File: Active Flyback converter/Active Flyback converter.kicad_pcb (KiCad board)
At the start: 12 copper layers, 114.5 x 43 mm, 0 parts

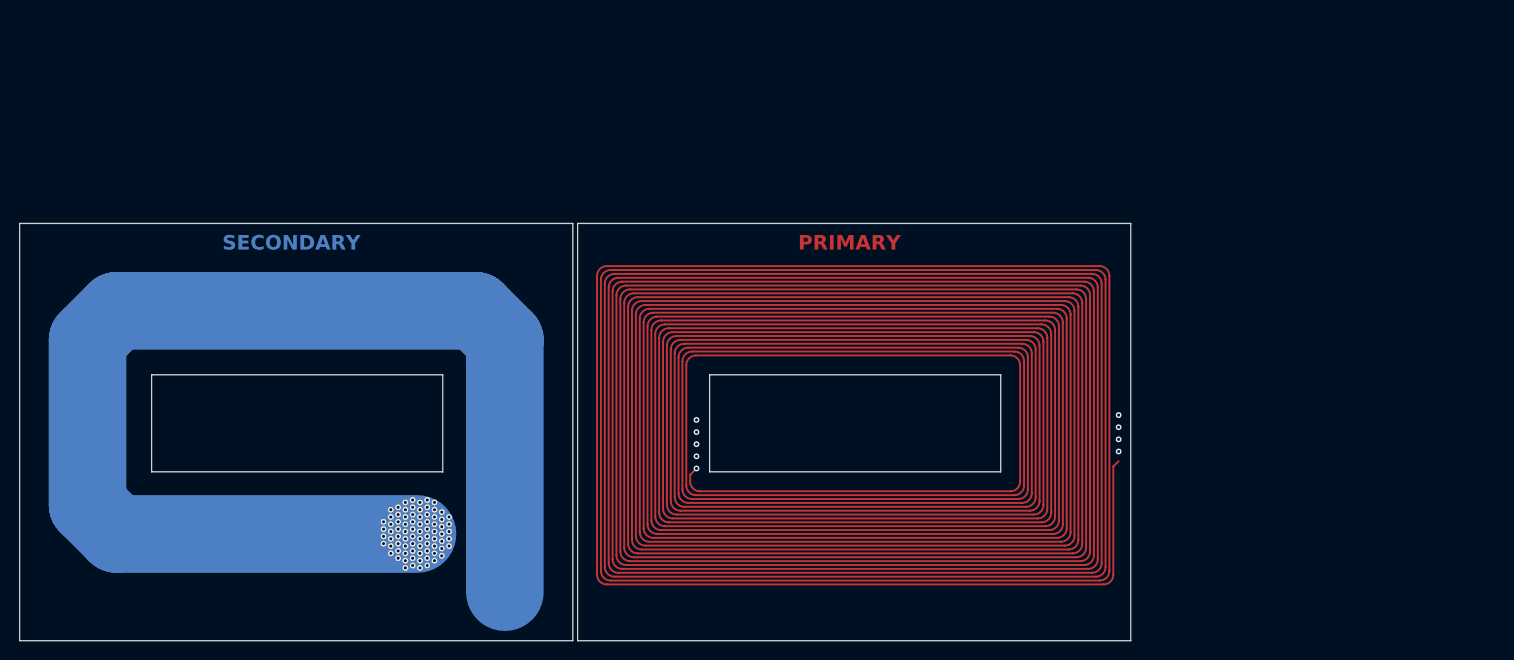
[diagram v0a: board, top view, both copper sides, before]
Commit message: Active flyback converter - v1.1
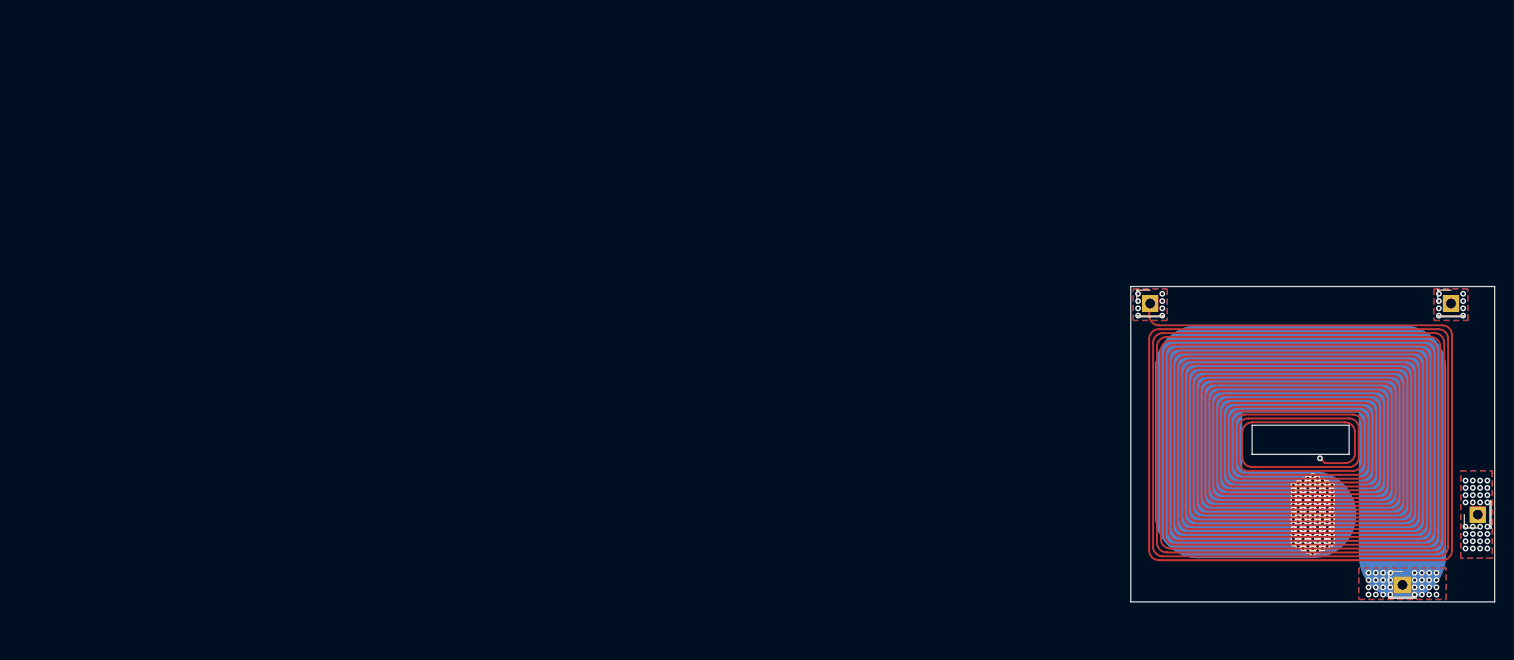
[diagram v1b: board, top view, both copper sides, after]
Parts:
- added J1: Conn_01x01_Pin, Connector_PinHeader_2.54mm:PinHeader_1x01_P2.54mm_Vertical, F.Cu at (157.0, 64.2)
- added J2: Conn_01x01_Pin, Connector_PinHeader_2.54mm:PinHeader_1x01_P2.54mm_Vertical, F.Cu at (190.8, 86.0)
- added J3: Conn_01x01_Pin, Connector_PinHeader_2.54mm:PinHeader_1x01_P2.54mm_Vertical, F.Cu at (188.0, 64.2)
- added J7: Conn_01x01_Pin, Connector_PinHeader_2.54mm:PinHeader_1x01_P2.54mm_Vertical, F.Cu at (183.0, 93.2)
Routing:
- net (no net): track 32506.6 -> 0.00 mm, vias 89 -> 0
- net /primary: track 0.00 -> 17714.3 mm, vias 0 -> 25
- net /secondary: track 0.00 -> 81.0 mm, vias 0 -> 197
- added copper zone on B.Cu, net /primary
- added copper zone on F.Cu, net /primary
- added copper zone on In1.Cu, net /primary
- added copper zone on In10.Cu, net /primary
- added copper zone on In2.Cu, net /primary
- added copper zone on In3.Cu, net /primary
- added copper zone on In4.Cu, net /primary
- added copper zone on In5.Cu, net /primary
- added copper zone on In6.Cu, net /primary
- added copper zone on In7.Cu, net /primary
- added copper zone on In8.Cu, net /primary
- added copper zone on In9.Cu, net /primary
- added copper zone on B.Cu, net /secondary
- added copper zone on F.Cu, net /secondary
- added copper zone on In1.Cu, net /secondary
- added copper zone on In10.Cu, net /secondary
- added copper zone on In2.Cu, net /secondary
- added copper zone on In3.Cu, net /secondary
- added copper zone on In4.Cu, net /secondary
- added copper zone on In5.Cu, net /secondary
- added copper zone on In6.Cu, net /secondary
- added copper zone on In7.Cu, net /secondary
- added copper zone on In8.Cu, net /secondary
- added copper zone on In9.Cu, net /secondary
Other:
- board size 114.5 x 43 mm -> 37.5 x 32.5 mm
- board text added: "250:1 planar transformer for 2.5V & 10A output. 1200V --> 2.1V 10A, 250KHz, 30% duty Np/Ns = (Vin * D) / (Vout * (1 - D)) = 245 Np = 245 turns, Ns = 1 turn L = ((u0 * N^2 * A) / l) Where... u0 = 4 * pi * 10^(-7) N = 250 (25 turns x 10 layers) A = 0.0325m x 0.01225m l = 0.0016m Thus, L = 19.543mH"
- board text removed: "PRIMARY"
- board text removed: "SECONDARY"

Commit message: Active flyback converter - v1.2
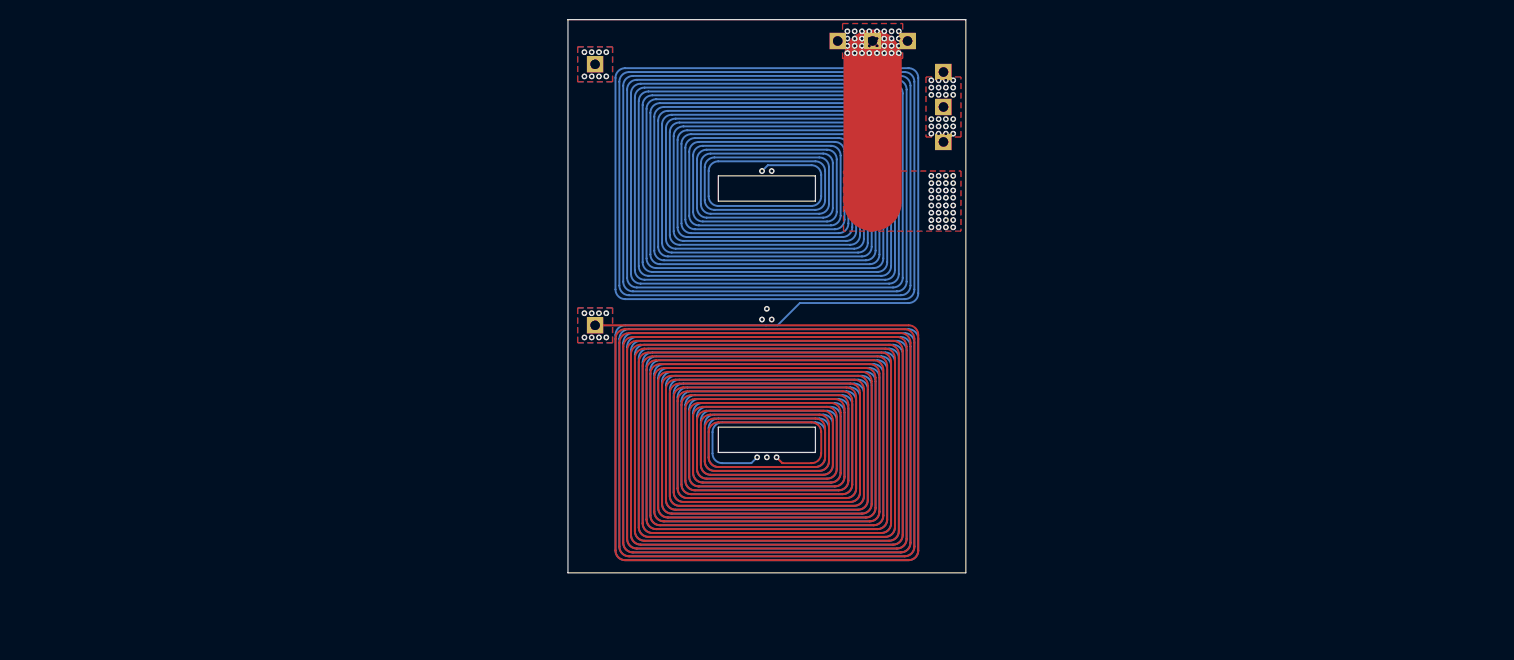
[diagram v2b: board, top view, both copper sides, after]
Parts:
- added J4: Conn_01x01_Pin, Connector_PinHeader_2.54mm:PinHeader_1x01_P2.54mm_Vertical, B.Cu at (135.7, 40.4)
- added J5: Conn_01x01_Pin, Connector_PinHeader_2.54mm:PinHeader_1x01_P2.54mm_Vertical, B.Cu at (135.7, 47.6)
- added J6: Conn_01x01_Pin, Connector_PinHeader_2.54mm:PinHeader_1x01_P2.54mm_Vertical, B.Cu at (132.0, 37.2)
- added J8: Conn_01x01_Pin, Connector_PinHeader_2.54mm:PinHeader_1x01_P2.54mm_Vertical, B.Cu at (124.8, 37.2)
- J1, J2, J3, J7: moved to B.Cu
- moved J3 91.6 mm to (99.8, 39.6), turned to 90 degrees
- moved J2 79.2 mm to (128.4, 37.2), turned to 0 degrees
- moved J7 68.3 mm to (135.7, 44.0), turned to 90 degrees
- moved J1 57.2 mm to (99.8, 66.5), turned to 90 degrees
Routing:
- net /primary: track 17714.3 -> 17771.2 mm, vias 25 -> 24
- net /secondary: track 81.0 -> 84.7 mm, vias 197 -> 88
- removed copper zone on In10.Cu, net /primary
- removed copper zone on In5.Cu, net /primary
- removed copper zone on In6.Cu, net /primary
- removed copper zone on In7.Cu, net /primary
- removed copper zone on In8.Cu, net /primary
- removed copper zone on In9.Cu, net /primary
- removed copper zone on B.Cu, net /secondary
- removed copper zone on In10.Cu, net /secondary
- removed copper zone on In2.Cu, net /secondary
- removed copper zone on In3.Cu, net /secondary
- removed copper zone on In4.Cu, net /secondary
- removed copper zone on In5.Cu, net /secondary
- removed copper zone on In6.Cu, net /secondary
- removed copper zone on In7.Cu, net /secondary
- removed copper zone on In8.Cu, net /secondary
- removed copper zone on In9.Cu, net /secondary
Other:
- board size 37.5 x 32.5 mm -> 41 x 57 mm
- copper layers 12 -> 6

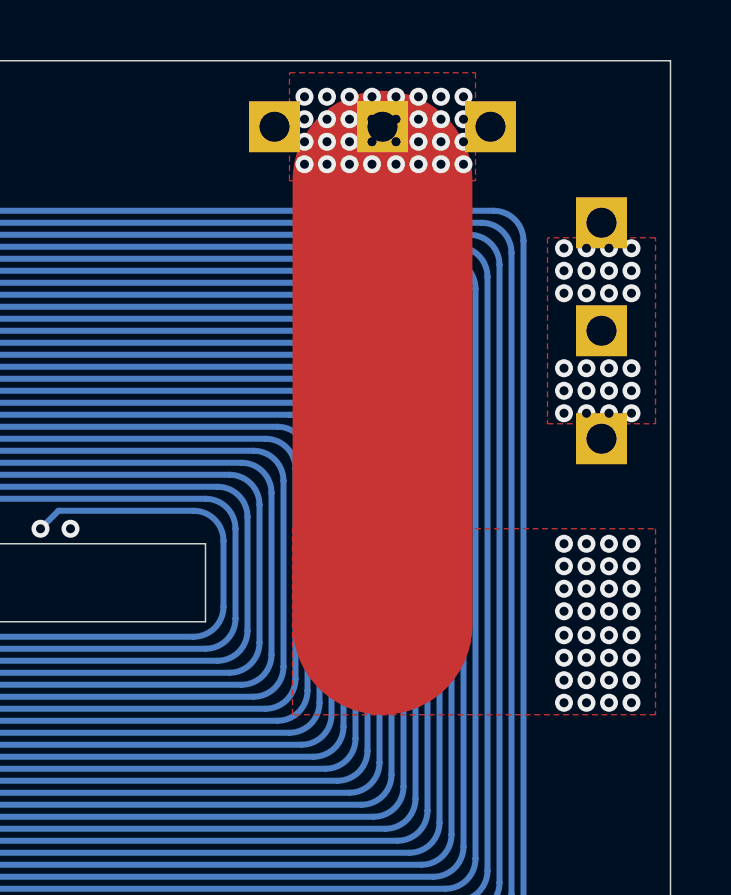
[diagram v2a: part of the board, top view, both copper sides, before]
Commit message: Active flyback converter (actual v1.2)
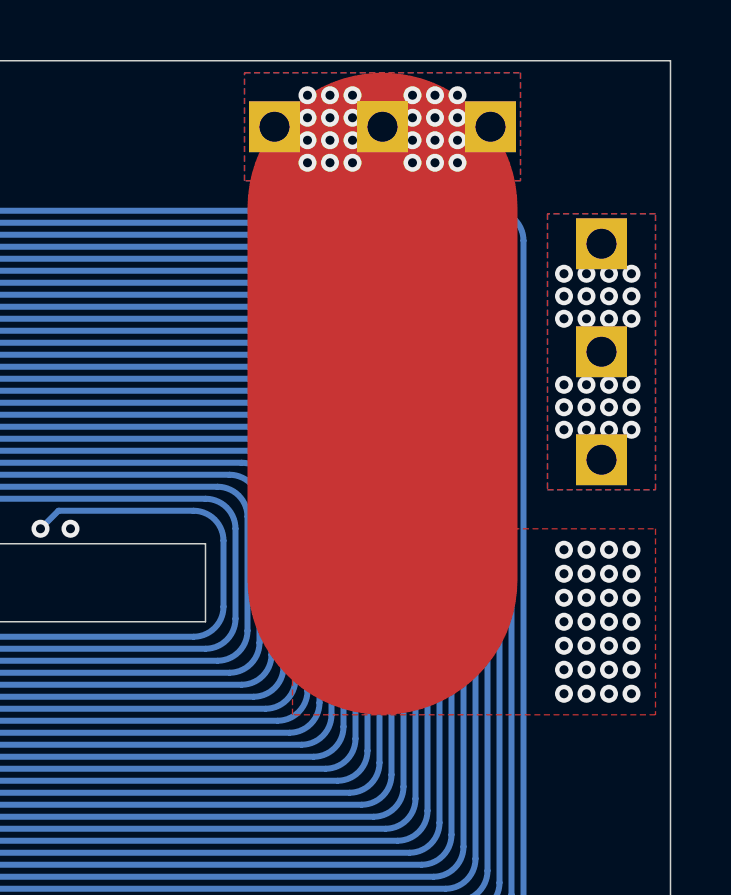
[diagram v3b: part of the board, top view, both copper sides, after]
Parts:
- moved J4 0.70 mm to (135.7, 41.1)
- moved J7 0.70 mm to (135.7, 44.7)
- moved J5 0.70 mm to (135.7, 48.3)
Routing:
- net /secondary: track 84.7 -> 78.2 mm, vias 88 -> 76
- added copper zone on B.Cu, net /secondary
- removed copper zone on In1.Cu, net /primary
- removed copper zone on In3.Cu, net /primary
- removed copper zone on In4.Cu, net /primary
